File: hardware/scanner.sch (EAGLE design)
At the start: 25 parts, among them K1 PIN20X2, U1 CAT24C32WI-GT3, U2 TPS61165DBV

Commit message: update board
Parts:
- removed R8: 10k, resistor:R-EU_M0805
- renumbered K1 to GPIO
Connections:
- net N$5 renamed LED_PWM
- net N$8 renamed LED_FB
- net N$9 renamed LED_SW
- net +5V: no longer R8.2
- net GND: now also LED1.3, LED2.3
- net TRIGGER: no longer R8.1
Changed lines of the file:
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@@
 </classes>
 <parts>
-<part name="K1" library="FLYFISH" deviceset="PIN20X2" device=""/>
+<part name="GPIO" library="FLYFISH" deviceset="PIN20X2" device=""/>
 <part name="FRAME1" library="frames" deviceset="A3L-LOC" device=""/>
 <part name="GND10" library="supply1" deviceset="GND" device=""/>
@@
 <part name="TRIGGER" library="con-molex" library_urn="urn:adsk.eagle:library:165" deviceset="22-?-03" device="05-7038"/>
 <part name="P+4" library="supply1" deviceset="+5V" device=""/>
-<part name="R8" library="resistor" deviceset="R-EU_" device="M0805" value="10k">
-<attribute name="TOLERANCE" value="5%"/>
-</part>
+<part name="GND13" library="supply1" deviceset="GND" device=""/>
 </parts>
 <sheets>
@@
 </plain>
 <instances>
-<instance part="K1" gate="G$1" x="83.82" y="152.4" smashed="yes" rot="R180">
+<instance part="GPIO" gate="G$1" x="83.82" y="152.4" smashed="yes" rot="R180">
 <attribute name="VALUE" x="87.63" y="180.34" size="1.778" layer="96" rot="R180"/>
 <attribute name="NAME" x="87.63" y="123.698" size="1.778" layer="95" rot="R180"/>
@@
 <attribute name="VALUE" x="93.98" y="106.68" size="1.778" layer="96" rot="R180"/>
 </instance>
-<instance part="R8" gate="G$1" x="99.06" y="93.98" smashed="yes" rot="R180">
-<attribute name="TOLERANCE" x="99.06" y="93.98" size="1.778" layer="96" rot="R180" display="off"/>
-<attribute name="NAME" x="98.8314" y="96.52" size="1.778" layer="95" rot="R90"/>
-<attribute name="VALUE" x="101.092" y="96.52" size="1.778" layer="96" rot="R90"/>
+<instance part="GND13" gate="1" x="177.8" y="170.18" smashed="yes">
+<attribute name="VALUE" x="175.26" y="167.64" size="1.778" layer="96"/>
 </instance>
 </instances>
@@
 </segment>
 <segment>
-<pinref part="K1" gate="G$1" pin="9"/>
+<pinref part="GPIO" gate="G$1" pin="9"/>
 <pinref part="GND3" gate="1" pin="GND"/>
 <wire x1="76.2" y1="165.1" x2="73.66" y2="165.1" width="0.1524" layer="91"/>
 <wire x1="73.66" y1="165.1" x2="73.66" y2="144.78" width="0.1524" layer="91"/>
-<pinref part="K1" gate="G$1" pin="25"/>
+<pinref part="GPIO" gate="G$1" pin="25"/>
 <wire x1="73.66" y1="144.78" x2="73.66" y2="127" width="0.1524" layer="91"/>
 <wire x1="73.66" y1="127" x2="73.66" y2="124.46" width="0.1524" layer="91"/>
 <wire x1="76.2" y1="144.78" x2="73.66" y2="144.78" width="0.1524" layer="91"/>
-<pinref part="K1" gate="G$1" pin="39"/>
+<pinref part="GPIO" gate="G$1" pin="39"/>
 <wire x1="76.2" y1="127" x2="73.66" y2="127" width="0.1524" layer="91"/>
 <junction x="73.66" y="144.78"/>
@@
 </segment>
 <segment>
-<pinref part="K1" gate="G$1" pin="6"/>
+<pinref part="GPIO" gate="G$1" pin="6"/>
 <pinref part="GND10" gate="1" pin="GND"/>
 <wire x1="91.44" y1="170.18" x2="93.98" y2="170.18" width="0.1524" layer="91"/>
 <wire x1="93.98" y1="170.18" x2="93.98" y2="160.02" width="0.1524" layer="91"/>
-<pinref part="K1" gate="G$1" pin="14"/>
+<pinref part="GPIO" gate="G$1" pin="14"/>
 <wire x1="93.98" y1="160.02" x2="93.98" y2="152.4" width="0.1524" layer="91"/>
 <wire x1="93.98" y1="152.4" x2="93.98" y2="139.7" width="0.1524" layer="91"/>
@@
 <wire x1="93.98" y1="134.62" x2="93.98" y2="124.46" width="0.1524" layer="91"/>
 <wire x1="91.44" y1="160.02" x2="93.98" y2="160.02" width="0.1524" layer="91"/>
-<pinref part="K1" gate="G$1" pin="20"/>
+<pinref part="GPIO" gate="G$1" pin="20"/>
 <wire x1="91.44" y1="152.4" x2="93.98" y2="152.4" width="0.1524" layer="91"/>
-<pinref part="K1" gate="G$1" pin="30"/>
+<pinref part="GPIO" gate="G$1" pin="30"/>
 <wire x1="91.44" y1="139.7" x2="93.98" y2="139.7" width="0.1524" layer="91"/>
-<pinref part="K1" gate="G$1" pin="34"/>
+<pinref part="GPIO" gate="G$1" pin="34"/>
 <wire x1="91.44" y1="134.62" x2="93.98" y2="134.62" width="0.1524" layer="91"/>
 <junction x="93.98" y="160.02"/>
@@
 <pinref part="GND4" gate="1" pin="GND"/>
 </segment>
+<segment>
+<pinref part="LED1" gate="G$1" pin="3"/>
+<pinref part="LED2" gate="G$1" pin="3"/>
+<wire x1="185.42" y1="180.34" x2="185.42" y2="170.18" width="0.1524" layer="91"/>
+<wire x1="185.42" y1="180.34" x2="177.8" y2="180.34" width="0.1524" layer="91"/>
+<junction x="185.42" y="180.34"/>
+<pinref part="GND13" gate="1" pin="GND"/>
+<wire x1="177.8" y1="180.34" x2="177.8" y2="172.72" width="0.1524" layer="91"/>
+</segment>
 </net>
 <net name="+3V3" class="0">
@@
 </segment>
 <segment>
-<pinref part="K1" gate="G$1" pin="1"/>
+<pinref part="GPIO" gate="G$1" pin="1"/>
 <pinref part="+3V1" gate="G$1" pin="+3V3"/>
 <wire x1="76.2" y1="175.26" x2="71.12" y2="175.26" width="0.1524" layer="91"/>
 <wire x1="71.12" y1="175.26" x2="71.12" y2="180.34" width="0.1524" layer="91"/>
-<pinref part="K1" gate="G$1" pin="17"/>
+<pinref part="GPIO" gate="G$1" pin="17"/>
 <wire x1="76.2" y1="154.94" x2="71.12" y2="154.94" width="0.1524" layer="91"/>
 <wire x1="71.12" y1="154.94" x2="71.12" y2="175.26" width="0.1524" layer="91"/>
@@
 <wire x1="93.98" y1="223.52" x2="101.6" y2="223.52" width="0.1524" layer="91"/>
 <wire x1="101.6" y1="223.52" x2="101.6" y2="226.06" width="0.1524" layer="91"/>
-<pinref part="K1" gate="G$1" pin="28"/>
+<pinref part="GPIO" gate="G$1" pin="28"/>
 <wire x1="91.44" y1="142.24" x2="101.6" y2="142.24" width="0.1524" layer="91"/>
 <wire x1="101.6" y1="142.24" x2="101.6" y2="223.52" width="0.1524" layer="91"/>
@@
 <net name="+5V" class="0">
 <segment>
-<pinref part="K1" gate="G$1" pin="2"/>
+<pinref part="GPIO" gate="G$1" pin="2"/>
 <pinref part="P+1" gate="1" pin="+5V"/>
 <wire x1="91.44" y1="175.26" x2="93.98" y2="175.26" width="0.1524" layer="91"/>
 <wire x1="93.98" y1="175.26" x2="93.98" y2="180.34" width="0.1524" layer="91"/>
-<pinref part="K1" gate="G$1" pin="4"/>
+<pinref part="GPIO" gate="G$1" pin="4"/>
 <wire x1="91.44" y1="172.72" x2="93.98" y2="172.72" width="0.1524" layer="91"/>
 <wire x1="93.98" y1="172.72" x2="93.98" y2="175.26" width="0.1524" layer="91"/>
@@
 <wire x1="91.44" y1="93.98" x2="91.44" y2="101.6" width="0.1524" layer="91"/>
 <pinref part="P+4" gate="1" pin="+5V"/>
-<pinref part="R8" gate="G$1" pin="2"/>
-<wire x1="91.44" y1="93.98" x2="93.98" y2="93.98" width="0.1524" layer="91"/>
-<junction x="91.44" y="93.98"/>
 </segment>
 </net>
@@
 <segment>
 <wire x1="88.9" y1="88.9" x2="106.68" y2="88.9" width="0.1524" layer="91"/>
-<wire x1="106.68" y1="88.9" x2="106.68" y2="93.98" width="0.1524" layer="91"/>
-<pinref part="K1" gate="G$1" pin="16"/>
-<wire x1="106.68" y1="93.98" x2="106.68" y2="157.48" width="0.1524" layer="91"/>
+<pinref part="GPIO" gate="G$1" pin="16"/>
+<wire x1="106.68" y1="88.9" x2="106.68" y2="157.48" width="0.1524" layer="91"/>
 <wire x1="106.68" y1="157.48" x2="91.44" y2="157.48" width="0.1524" layer="91"/>
 <pinref part="TRIGGER" gate="-3" pin="S"/>
-<pinref part="R8" gate="G$1" pin="1"/>
-<wire x1="104.14" y1="93.98" x2="106.68" y2="93.98" width="0.1524" layer="91"/>
-<junction x="106.68" y="93.98"/>
-</segment>
-</net>
-<net name="N$5" class="0">
-<segment>
-<pinref part="K1" gate="G$1" pin="12"/>
+</segment>
+</net>
+<net name="LED_PWM" class="0">
+<segment>
+<pinref part="GPIO" gate="G$1" pin="12"/>
 <wire x1="91.44" y1="162.56" x2="132.08" y2="162.56" width="0.1524" layer="91"/>
 <pinref part="U2" gate="G$1" pin="CTRL"/>
@@
 <wire x1="93.98" y1="220.98" x2="111.76" y2="220.98" width="0.1524" layer="91"/>
 <pinref part="U1" gate="A" pin="SCL"/>
-<pinref part="K1" gate="G$1" pin="27"/>
+<pinref part="GPIO" gate="G$1" pin="27"/>
 <wire x1="76.2" y1="142.24" x2="66.04" y2="142.24" width="0.1524" layer="91"/>
 <wire x1="66.04" y1="142.24" x2="66.04" y2="111.76" width="0.1524" layer="91"/>
@@
 </segment>
 </net>
-<net name="N$8" class="0">
+<net name="LED_FB" class="0">
 <segment>
 <pinref part="U2" gate="G$1" pin="FB"/>
@@
 </segment>
 </net>
-<net name="N$9" class="0">
+<net name="LED_SW" class="0">
 <segment>
 <pinref part="U2" gate="G$1" pin="SW"/>
@@
 <net name="LED4" class="0">
 <segment>
-<pinref part="K1" gate="G$1" pin="13"/>
+<pinref part="GPIO" gate="G$1" pin="13"/>
 <wire x1="76.2" y1="160.02" x2="55.88" y2="160.02" width="0.1524" layer="91"/>
 <pinref part="R6" gate="G$1" pin="1"/>
@@
 <net name="LED3" class="0">
 <segment>
-<pinref part="K1" gate="G$1" pin="11"/>
+<pinref part="GPIO" gate="G$1" pin="11"/>
 <wire x1="76.2" y1="162.56" x2="58.42" y2="162.56" width="0.1524" layer="91"/>
 <wire x1="58.42" y1="162.56" x2="58.42" y2="167.64" width="0.1524" layer="91"/>
@@
 <net name="LED5" class="0">
 <segment>
-<pinref part="K1" gate="G$1" pin="15"/>
+<pinref part="GPIO" gate="G$1" pin="15"/>
 <wire x1="76.2" y1="157.48" x2="58.42" y2="157.48" width="0.1524" layer="91"/>
 <wire x1="58.42" y1="157.48" x2="58.42" y2="152.4" width="0.1524" layer="91"/>

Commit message: final layout?
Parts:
- R3: value 1k -> 3k9
- R4: value 0.57 -> 0.56
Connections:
- net LED_PWM renamed LED_CTRL
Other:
- note added: "v1.0"
- note removed: "v0.1"
- moved on the sheet: C2, C3, C4, D1, L1, LED1, LED2, R4, U2

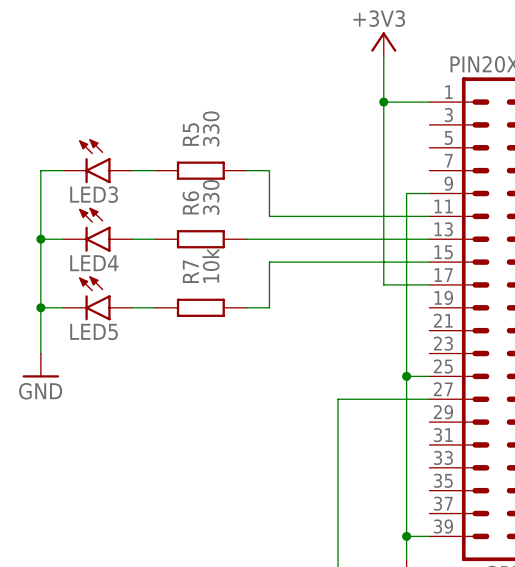
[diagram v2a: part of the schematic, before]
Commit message: address drc complaints, fixed font
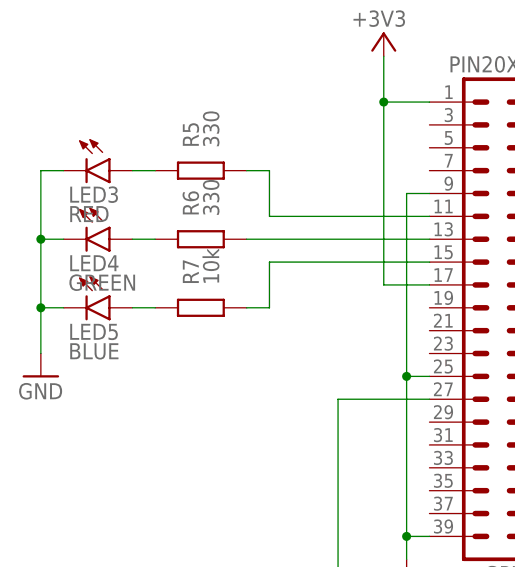
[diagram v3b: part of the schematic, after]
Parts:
- LED3: value (none) -> RED
- LED4: value (none) -> GREEN
- LED5: value (none) -> BLUE
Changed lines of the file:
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@@
 <part name="LED1" library="LW_W5SM-JYKY-JKQL-1" deviceset="LW_W5SM-JYKY-JKQL-1" device=""/>
 <part name="LED2" library="LW_W5SM-JYKY-JKQL-1" deviceset="LW_W5SM-JYKY-JKQL-1" device=""/>
-<part name="LED3" library="led" library_urn="urn:adsk.eagle:library:259" deviceset="LED" device="CHIP-LED0805" package3d_urn="urn:adsk.eagle:package:15818/2"/>
+<part name="LED3" library="led" library_urn="urn:adsk.eagle:library:259" deviceset="LED" device="CHIP-LED0805" package3d_urn="urn:adsk.eagle:package:15818/2" value="RED"/>
 <part name="R5" library="resistor" deviceset="R-EU_" device="M0805" value="330">
 <attribute name="TOLERANCE" value="5%"/>
 </part>
 <part name="GND12" library="supply1" deviceset="GND" device=""/>
-<part name="LED4" library="led" library_urn="urn:adsk.eagle:library:259" deviceset="LED" device="CHIP-LED0805" package3d_urn="urn:adsk.eagle:package:15818/2"/>
+<part name="LED4" library="led" library_urn="urn:adsk.eagle:library:259" deviceset="LED" device="CHIP-LED0805" package3d_urn="urn:adsk.eagle:package:15818/2" value="GREEN"/>
 <part name="R6" library="resistor" deviceset="R-EU_" device="M0805" value="330">
 <attribute name="TOLERANCE" value="5%"/>
 </part>
-<part name="LED5" library="led" library_urn="urn:adsk.eagle:library:259" deviceset="LED" device="CHIP-LED0805" package3d_urn="urn:adsk.eagle:package:15818/2"/>
+<part name="LED5" library="led" library_urn="urn:adsk.eagle:library:259" deviceset="LED" device="CHIP-LED0805" package3d_urn="urn:adsk.eagle:package:15818/2" value="BLUE"/>
 <part name="R7" library="resistor" deviceset="R-EU_" device="M0805" value="10k">
 <attribute name="TOLERANCE" value="5%"/>
@@
 </sheet>
 </sheets>
+<errors>
+</errors>
 </schematic>
 </drawing>
